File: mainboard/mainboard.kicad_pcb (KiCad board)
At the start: 2 copper layers, 44.3 x 46.2 mm, 107 parts, among them J1 USB_B_Micro, J2 Conn_01x19_MountingPin, J3 Conn_01x19_MountingPin, J4 Conn_01x02_MountingPin, Q1 DMG2301L, Q2 MMBT3904, Q3 MMBT3904, SW1 SW_Push, SW2 SW_Push, U1 ESP32-WROOM-32, U2 tps63070, U3 tps63070, U4 tps63070, U5 CP2102N-A01-GQFN24, U6 BME680, U7 BH1750FVI, U8 LIS3MDL, U9 ADXL343

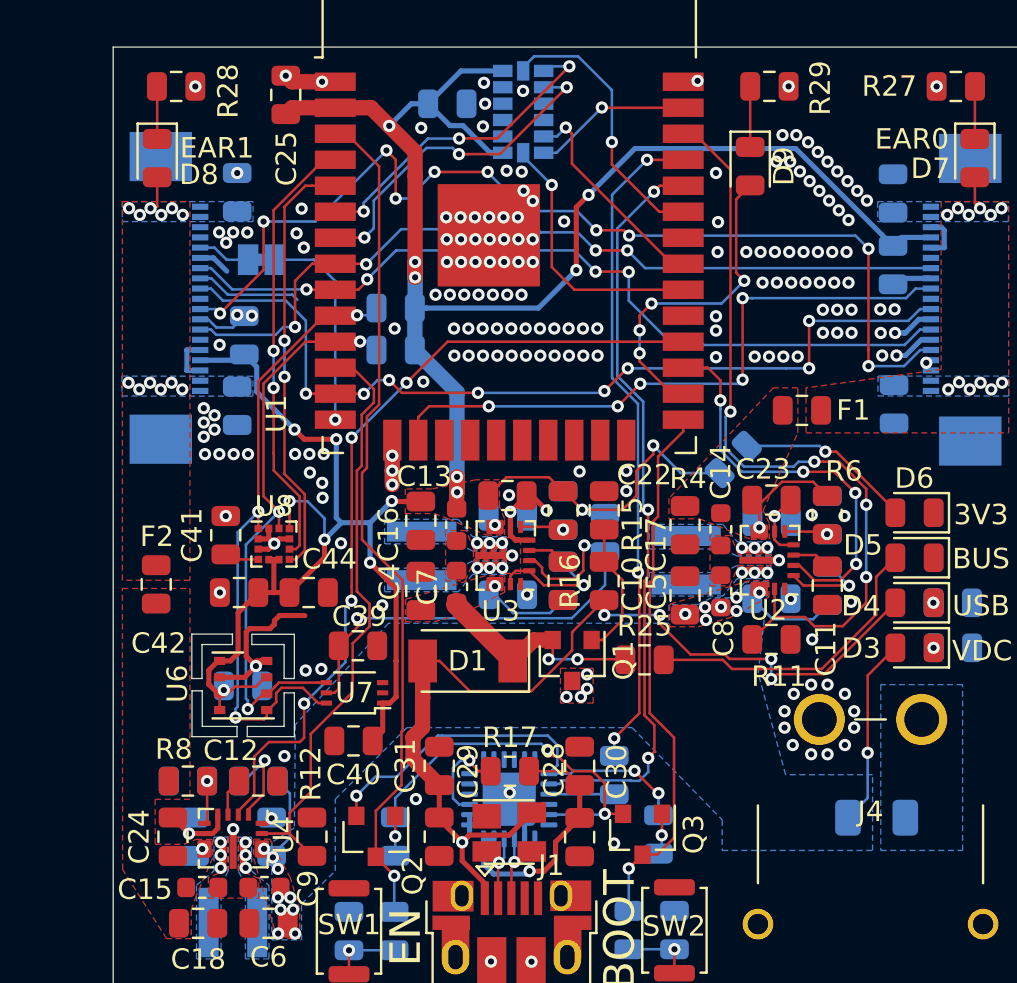
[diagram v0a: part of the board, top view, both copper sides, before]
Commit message: Reassign silkscreen designators
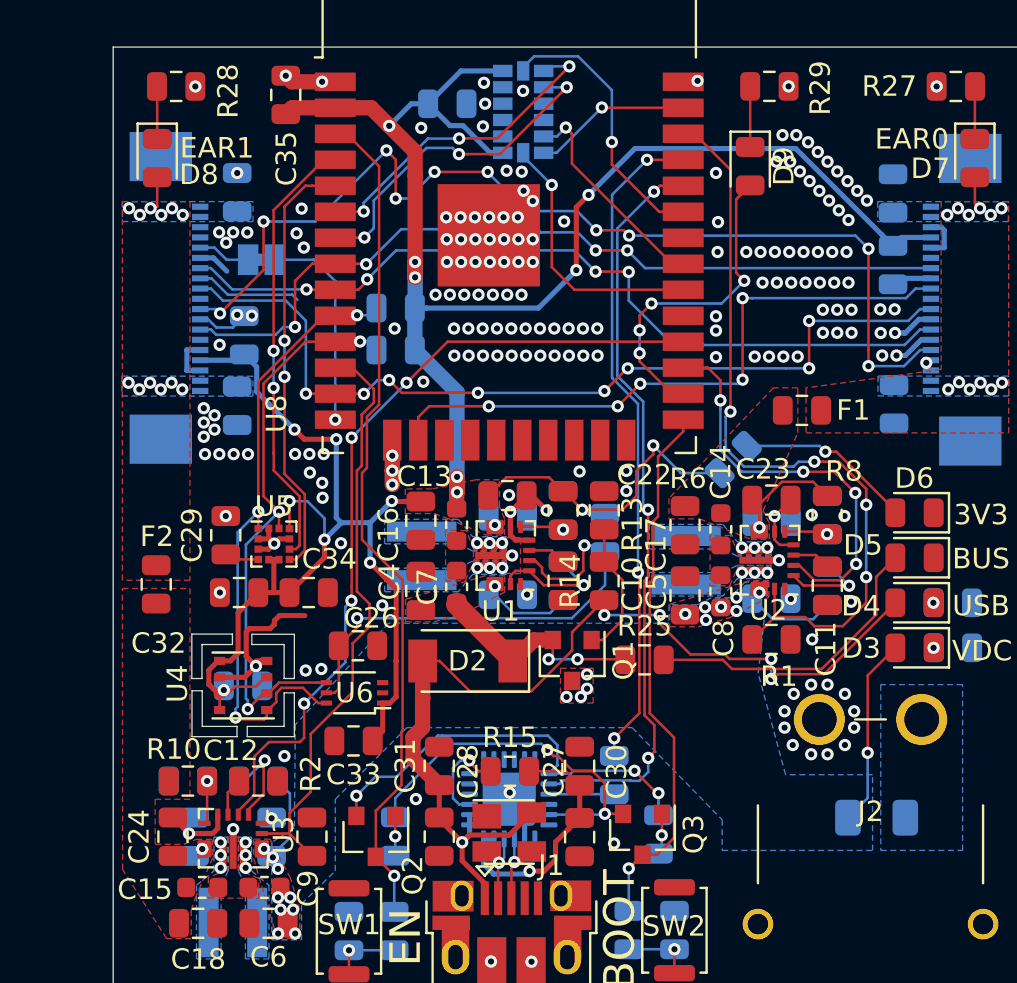
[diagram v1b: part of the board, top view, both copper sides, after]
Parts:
- renumbered C38 to C25, C39 to C26, C28 to C27, C29 to C28, C41 to C29, C42 to C32, C40 to C33, C44 to C34, C25 to C35, C43 to C36, C36 to C37, C37 to C38, C26 to C39, C27 to C40, C32 to C41, C33 to C42, C34 to C43, C35 to C44, D2 to D1, D1 to D2, F4 to F3, J4 to J2, J2 to J3, J3 to J4, JP4 to JP1, R11 to R1, R8 to R10, R9 to R11, R10 to R12, R15 to R13, R16 to R14, R17 to R15, R18 to R16, R19 to R17, R20 to R18, R13 to R19, R12 to R2, R14 to R20, R1 to R3, R2 to R4, R3 to R5, R4 to R6, R5 to R7, R6 to R8, R7 to R9, U3 to U1, U4 to U3, U6 to U4, U8 to U5, U7 to U6, U5 to U7, U1 to U8
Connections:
- U8 pad 39: (no net) -> GND
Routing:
- net GND: vias 173 -> 195
- net (no net): vias 22 -> 0

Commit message: More ground stitching
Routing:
- net GND: vias 195 -> 215
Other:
- board text added: "Tobias Schramm 2019"

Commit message: Add revision indicator
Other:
- board text added: "Rev A"
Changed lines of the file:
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@@
   (general
     (thickness 1.6)
-    (drawings 40)
+    (drawings 41)
     (tracks 1223)
     (zones 0)
@@
     )
   )
+  (gr_text "Rev A" (at 91 122 90) (layer F.SilkS)
+    (effects (font (size 1 1) (thickness 0.15)))
+  )
   (gr_text "Tobias\nSchramm\n2019" (at 89.35 117.3 90) (layer F.SilkS)

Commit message: Replace reset circuitry
It was the reference circuit used on the DevKitC V4 but it just plain does not work.
Replaced by much simpler and more reliable design.
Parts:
- added R30: 10 kR, Resistor_SMD:R_0805_2012Metric, B.Cu at (72.4, 86.7)
- added R31: 10 kR, Resistor_SMD:R_0805_2012Metric, B.Cu at (88.5, 102.3)
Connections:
- Q2 pad 2: /RTS -> GND
- Q3 pad 2: /DTR -> GND
- R17 pad 2: /DTR -> /RTS
- R18 pad 2: /RTS -> /DTR
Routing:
- net /DTR: track 18.2 -> 5.37 mm, vias 2 -> 0
- net /RTS: track 20.8 -> 12.5 mm, vias 3 -> 0
- net +3V3: track 139.6 -> 142.2 mm
- net /EN: track 41.3 -> 42.6 mm, vias 1 -> 2
- net /IO0: track 26.5 -> 27.1 mm, vias 1 -> 2
- net GND: track 55.0 -> 55.1 mm, vias 215 -> 218
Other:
- board text added: "Rev B"
- board text removed: "Rev A"

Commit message: Revert "Replace reset circuitry"
This reverts commit 4aa51ba1305b71722c80cb68cdfb79191ae487c4.

CP2102N defaults to RTS + CTS high. Thus the reference reset circuitry is the only
simple way to make this work
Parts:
- removed R30, R31: 10 kR, Resistor_SMD:R_0805_2012Metric
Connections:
- Q2 pad 2: GND -> /RTS
- Q3 pad 2: GND -> /DTR
- R17 pad 2: /RTS -> /DTR
- R18 pad 2: /DTR -> /RTS
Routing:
- net /DTR: track 5.37 -> 18.2 mm, vias 0 -> 2
- net /RTS: track 12.5 -> 20.8 mm, vias 0 -> 3
- net +3V3: track 142.2 -> 139.6 mm
- net /EN: track 42.6 -> 41.3 mm, vias 2 -> 1
- net /IO0: track 27.1 -> 26.5 mm, vias 2 -> 1
- net GND: track 55.1 -> 55.0 mm, vias 218 -> 215
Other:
- board text added: "Rev A"
- board text removed: "Rev B"

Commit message: Add measurements for 3d case
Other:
- board text added: "Auflageflächen liegen auf der Ebene Eco2.User (gelb). Auflageflächen, welche unmittelbar in den Platinenecken liegen (links unten, links oben, rechts oben) dürfen sich bis zum Platinenrand erstrecken. Maximale Höhe Platinenoberseite: 5 mm Dicke Platinenmaterial: 1,6 mm Maximal Höhe Platinenunterseite: 2 mm"

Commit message: More measurements for top
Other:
- board text added: "Auflageflächen auf der Platinenoberseite liegen auf Ebene Eco1.User (grün) und haben gelbe Bemaßungen. Bereichre, welche auf Dwgs.User (hellgrau) markiert sind sind Löcher. Diese Bereiche sollten auf der Gehäuseoberseite frei gehalten werden."
- board text added: "Auflageflächen auf der Platinenunterseite liegen auf der Ebene Eco2.User (gelb). Auflageflächen, welche unmittelbar in den Platinenecken liegen (links unten, links oben, rechts oben) dürfen sich bis zum Platinenrand erstrecken. Maximale Höhe Platinenoberseite: 5 mm Dicke Platinenmaterial: 1,6 mm Maximal Höhe Platinenunterseite: 2 mm"
- board text added: "Micro USB B Buchse, Nptwendige Höhe für Loch auf Platinenoberseite: 3 mm"
- board text added: "XT30PW Buchse, Höhe des notwendigen Lochs: 5 mm"
- board text removed: "Auflageflächen liegen auf der Ebene Eco2.User (gelb). Auflageflächen, welche unmittelbar in den Platinenecken liegen (links unten, links oben, rechts oben) dürfen sich bis zum Platinenrand erstrecken. Maximale Höhe Platinenoberseite: 5 mm Dicke Platinenmaterial: 1,6 mm Maximal Höhe Platinenunterseite: 2 mm"

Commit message: Even more measurements for reduced readability
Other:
- board text added: "r = 1,5"
